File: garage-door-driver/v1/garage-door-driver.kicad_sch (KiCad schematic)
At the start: 5 parts, among them J1 Screw_Terminal_01x04

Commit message: wip sch
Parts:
- removed D1: LED_ARGB, mylife-footprints:LED RGB 10W, symbol Device:LED_ARGB
- removed J1: Screw_Terminal_01x04, mylife-footprints:RS PRO Terminal Small x4, symbol Connector:Screw_Terminal_01x04
- removed R1, R2: 5.1Ω/1W, Resistor_SMD:R_2512_6332Metric, symbol Device:R
- removed R3: 10Ω/1W, Resistor_SMD:R_2512_6332Metric, symbol Device:R
- added J1, J3: Screw_Terminal_01x02, symbol Connector:Screw_Terminal_01x02
- added J2: Conn_01x07_Pin, symbol Connector:Conn_01x07_Pin
- added U1: WeMos_D1_mini, Module:WEMOS_D1_mini_light, symbol MCU_Module:WeMos_D1_mini
- added U2: 4N35, Package_DIP:DIP-6_W7.62mm, symbol Isolator:4N35

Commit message: sch
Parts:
- added D1, D2, D3, D4, D5: LED, Diode_SMD:D_0805_2012Metric, symbol Device:LED
- added J4: Conn_01x03_Male, Connector_PinHeader_2.54mm:PinHeader_1x03_P2.54mm_Vertical, symbol Connector:Conn_01x03_Male
- added R1, R12, R13, R6, R8: 1KΩ, Resistor_SMD:R_0603_1608Metric, symbol Device:R
- added R10, R11, R4: 2.2KΩ, Resistor_SMD:R_0603_1608Metric, symbol Device:R
- added R14, R3: 220Ω, Resistor_SMD:R_0603_1608Metric, symbol Device:R
- added R2, R7, R9: 10KΩ, Resistor_SMD:R_0603_1608Metric, symbol Device:R
- added R5: 4.7KΩ, Resistor_SMD:R_0402_1005Metric, symbol Device:R
- added U3, U4, U5, U6: 4N35, Package_DIP:DIP-6_W7.62mm, symbol Isolator:4N35
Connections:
- net at J3.1 (Pin_1): now also R10.1
- net at J3.2 (Pin_2): now also U4.2
- net at U2.1: now also R4.2
- net at U2.2: now also J1.1 (Pin_1), R11.1
- net GND: now reaches U2.4
- net GND: now also U1.10 (GND), J4.1 (Pin_1), R12.1, R13.1, U3.4, U4.4, U5.2, U5.4, U6.2, U6.4
- net at U2.5: now also U1.4 (SCK/D5), R1.1, R2.1
- net at J1.2 (Pin_2): now also R4.1, U3.2
- net at U1.11 (D4): now also D5.2 (A), R3.1
- net at U1.12 (D3): now also D4.2 (A), R14.1
- net at U1.15 (RX): now also J4.3 (Pin_3), R5.2
- net at U1.5 (MISO/D6): now also R6.1, R7.1, U3.5
- net at U1.6 (MOSI/D7): now also R8.1, R9.1, U4.5
- net +3V3: now reaches U1.8 (3V3)
- net +3V3: now also D1.2 (A), D2.2 (A), D3.2 (A), J4.2 (Pin_2), R2.2, R5.1, R7.2, R9.2
- net +5V: now reaches U1.9 (5V)
- new net: R3.2, U6.1
- new net: R11.2, U3.1
- new net: D1.1 (K), R1.2
- new net: D3.1 (K), R8.2
- new net: D2.1 (K), R6.2
- new net: D5.1 (K), R13.2
- new net: R10.2, U4.1
- new net: D4.1 (K), R12.2
- new net: R14.2, U5.1
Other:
- note added: "24v"
- note added: "Bornier noir"
- note added: "DS18B20"
- note added: "GND"
- note added: "Moteur"
- note added: "VCC"
- note added: "data"
- moved on the sheet: J1, J2, J3, U1, U2

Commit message: sch
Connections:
- net GND: now also J2.1 (Pin_1)
- net at U6.5: now also J2.3 (Pin_3)
- net +24V: now reaches J2.5 (Pin_5)
- net at J2.7 (Pin_7): now also U5.5
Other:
- note added: "20 21 5 23"
- note added: "Bornier droite"
- note added: "D5 : in moteur (active low) D6 : in moteur (active low) D7 : in porte fermée (active low) D3 : out ouverture partielle D4 : out ouverture totale RX : DS18B20"
- moved on the sheet: J4, R5

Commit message: sch
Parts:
- added C1: 10μF/50V, Capacitor_SMD:C_1206_3216Metric, symbol Device:C_Polarized
- added C2: 22μF/10V, Capacitor_SMD:C_0805_2012Metric, symbol Device:C_Polarized
- added U7: R-785.0-1.0, Converter_DCDC:Converter_DCDC_RECOM_R-78E-0.5_THT, symbol Regulator_Switching:R-785.0-1.0
- U2, U3, U4, U5, U6: footprint Package_DIP:DIP-6_W7.62mm -> Package_DIP:DIP-6_W8.89mm_SMDSocket_LongPads; LCSC (none) -> C500385
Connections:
- net +24V: now also C1.1, U7.1 (IN)
- net +5V: now also C2.1, U7.3 (OUT)
- net GND: now also C1.2, C2.2, U7.2 (GND)

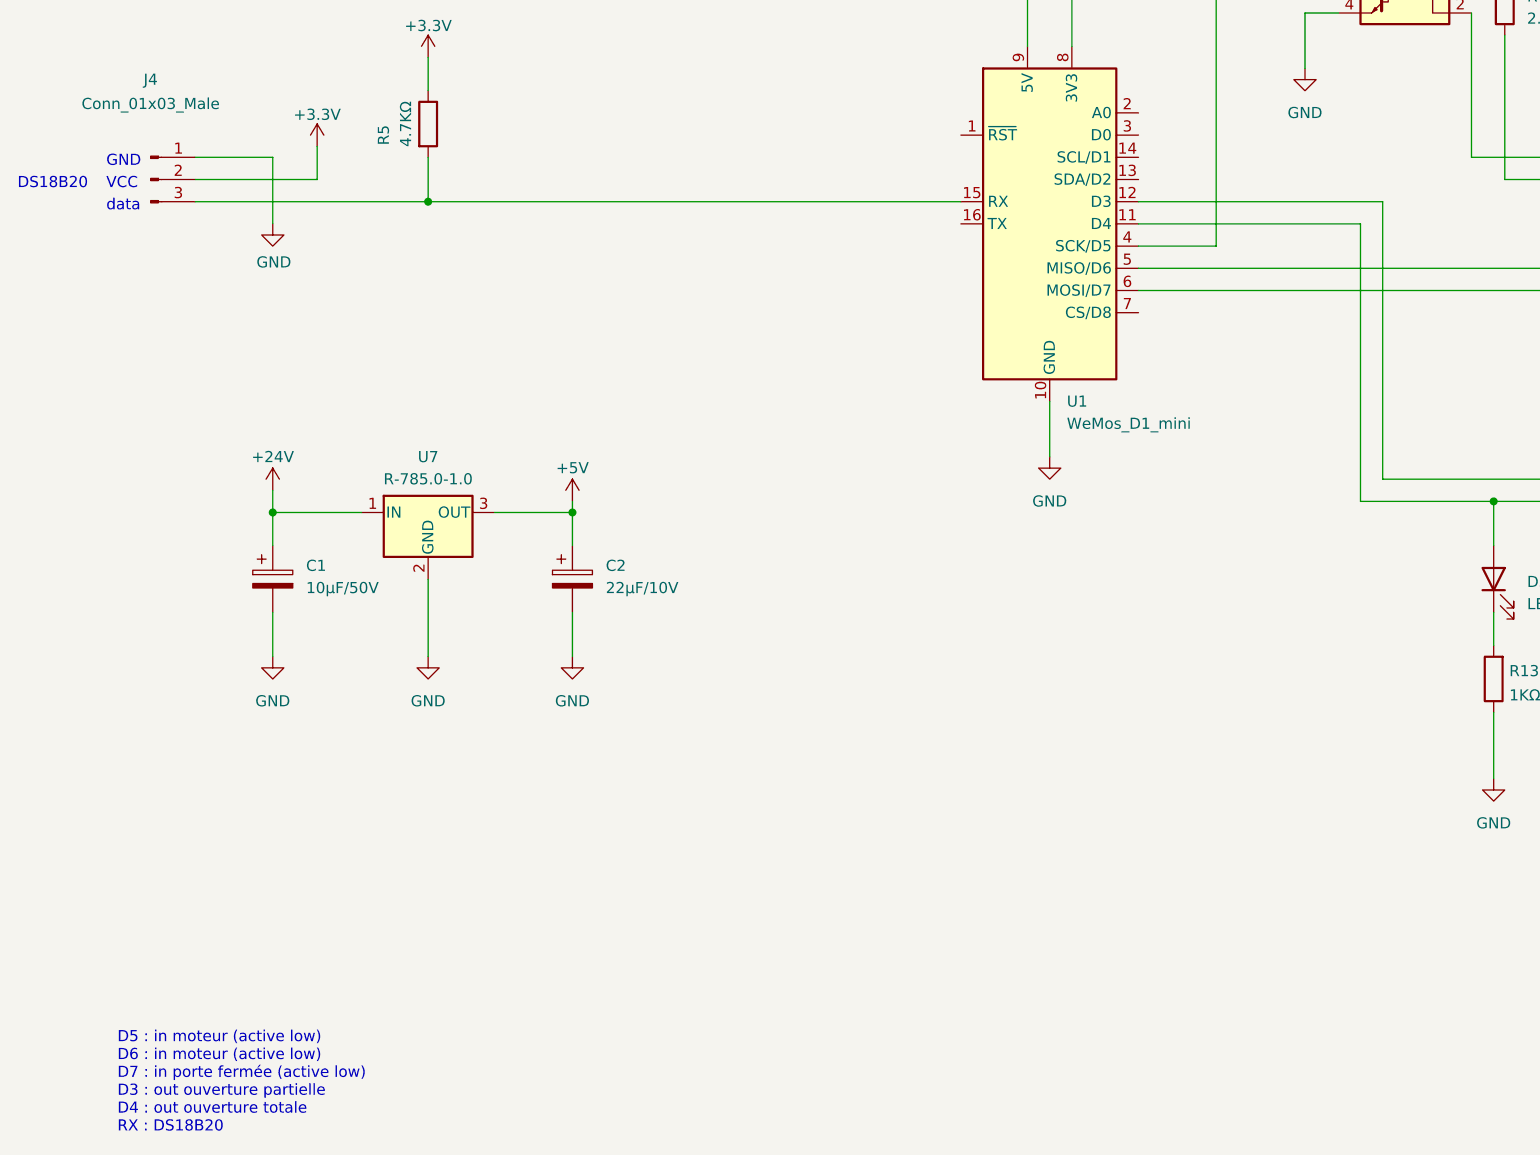
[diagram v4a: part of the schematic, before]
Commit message: fix esp8366 used pins
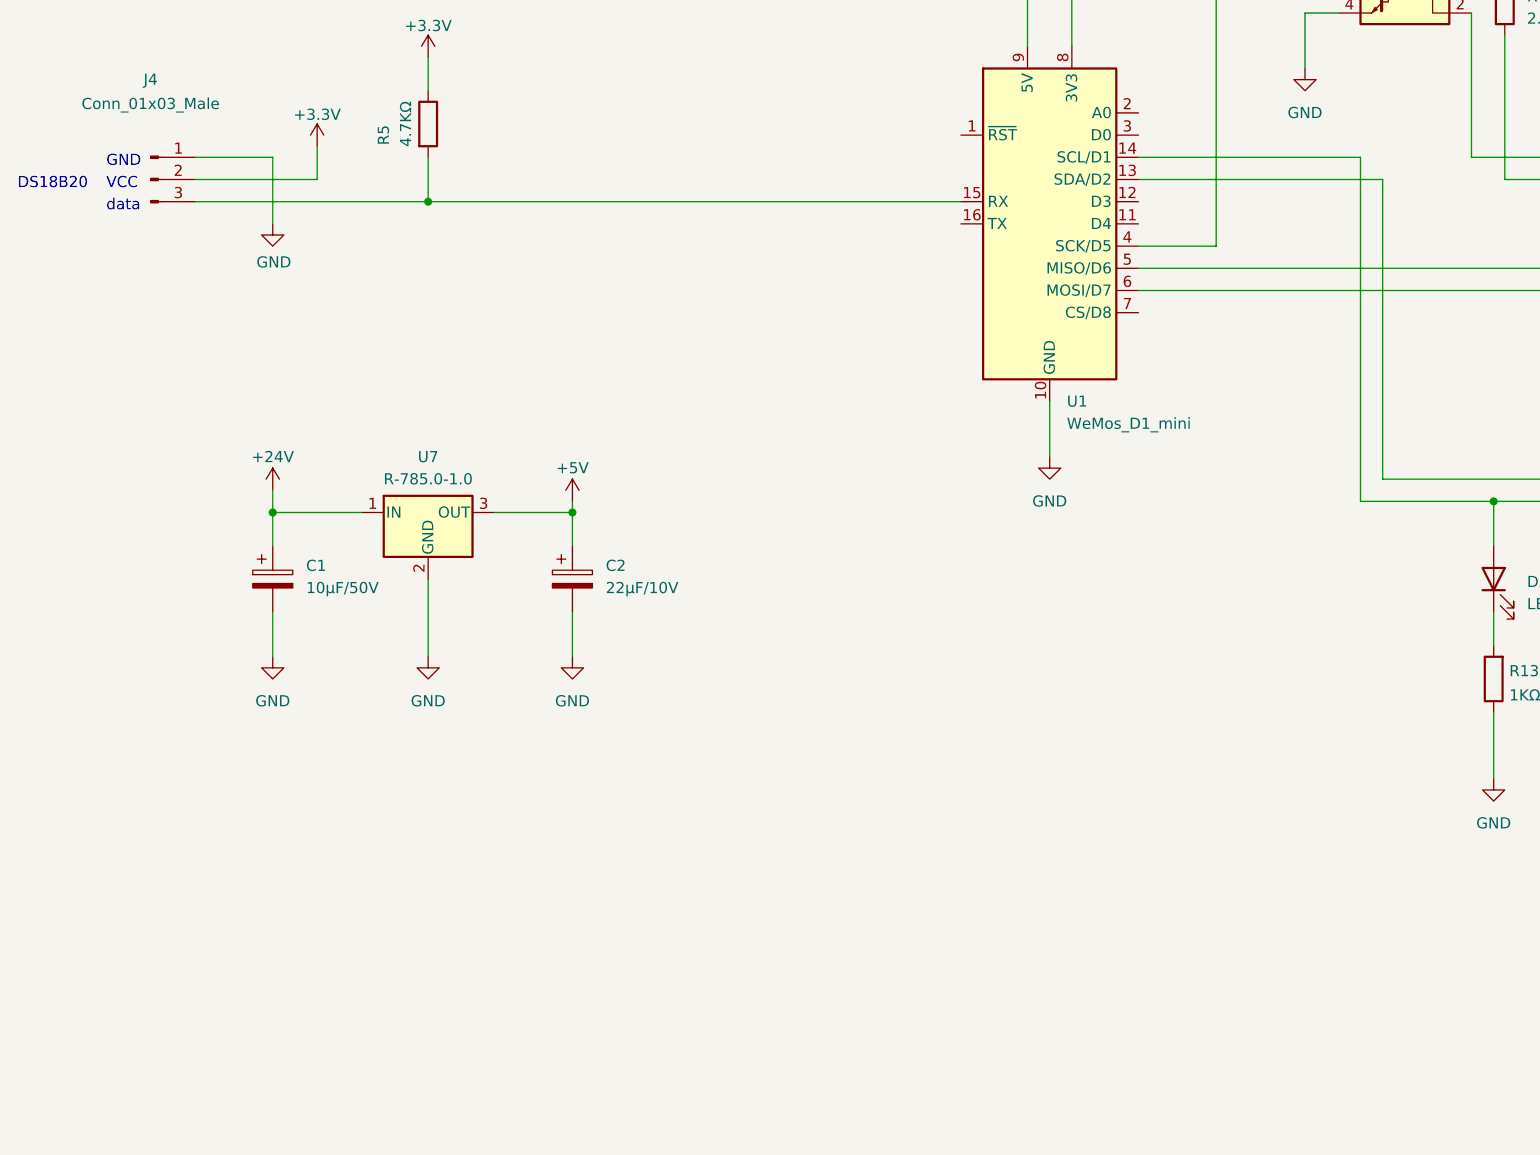
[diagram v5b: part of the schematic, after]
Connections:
- net at D5.2 (A), R3.1: now also U1.14 (SCL/D1); no longer U1.11 (D4)
- net at D4.2 (A), R14.1: now also U1.13 (SDA/D2); no longer U1.12 (D3)
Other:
- note removed: "D5 : in moteur (active low) D6 : in moteur (active low) D7 : in porte fermée (active low) D3 : out ouverture partielle D4 : out ouverture totale RX : DS18B20"
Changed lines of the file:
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@@
+    (stroke (width 0) (type default))
+  )
+  (wire (pts (xy 161.29 91.44) (xy 186.69 91.44))
     (stroke (width 0) (type default))
   )
@@
     (stroke (width 0) (type default))
   )
-  (wire (pts (xy 189.23 96.52) (xy 189.23 128.27))
-    (stroke (width 0) (type default))
-  )
   (wire (pts (xy 213.36 67.31) (xy 213.36 63.5))
     (stroke (width 0) (type default))
@@
     (stroke (width 0) (type default))
   )
+  (wire (pts (xy 189.23 93.98) (xy 189.23 128.27))
+    (stroke (width 0) (type default))
+  )
   (wire (pts (xy 302.26 93.98) (xy 242.57 93.98))
     (stroke (width 0) (type default))
@@
     (stroke (width 0) (type default))
   )
-  (wire (pts (xy 186.69 99.06) (xy 186.69 130.81))
+  (wire (pts (xy 186.69 91.44) (xy 186.69 130.81))
     (stroke (width 0) (type default))
   )
@@
     (stroke (width 0) (type default))
   )
+  (wire (pts (xy 161.29 93.98) (xy 189.23 93.98))
+    (stroke (width 0) (type default))
+  )
   (wire (pts (xy 96.52 143.51) (xy 96.52 148.59))
     (stroke (width 0) (type default))
@@
     (stroke (width 0) (type default))
   )
-  (wire (pts (xy 161.29 99.06) (xy 186.69 99.06))
-    (stroke (width 0) (type default))
-  )
   (wire (pts (xy 256.54 106.68) (xy 256.54 67.31))
     (stroke (width 0) (type default))
@@
     (stroke (width 0) (type default))
   )
-  (wire (pts (xy 161.29 96.52) (xy 189.23 96.52))
-    (stroke (width 0) (type default))
-  )
   (wire (pts (xy 304.8 128.27) (xy 285.75 128.27))
     (stroke (width 0) (type default))
@@
     (effects (font (size 1.27 1.27)) (justify left bottom))
   )
-  (text "D5 : in moteur (active low)\nD6 : in moteur (active low)\nD7 : in porte fermée (active low)\nD3 : out ouverture partielle\nD4 : out ouverture totale\nRX : DS18B20"
-    (at 44.45 203.2 0)
-    (effects (font (size 1.27 1.27)) (justify left bottom))
-  )

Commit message: annotate
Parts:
- renumbered D5 to D2, D2 to D3, D3 to D5, J4 to J1, J3 to J2, J1 to J3, J2 to J4, R5 to R1, R11 to R10, R14 to R11, R8 to R12, R9 to R13, R10 to R14, R1 to R2, R2 to R3, R13 to R4, R4 to R5, R3 to R7, R7 to R8, R12 to R9, U7 to U1, U1 to U2, U2 to U3, U6 to U4, U3 to U5, U5 to U6, U4 to U7

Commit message: pcb
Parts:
- J2, J3: footprint (none) -> mylife-footprints:RS PRO Terminal Small x2
- J4: footprint (none) -> Connector_PinHeader_2.54mm:PinHeader_1x07_P2.54mm_Vertical
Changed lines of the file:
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@@
       (effects (font (size 1.27 1.27)) (justify left))
     )
-    (property "Footprint" "" (at 307.34 69.85 0)
-      (effects (font (size 1.27 1.27)) hide)
-    )
-    (property "Datasheet" "~" (at 307.34 69.85 0)
+    (property "Footprint" "mylife-footprints:RS PRO Terminal Small x2" (at 307.34 69.85 0)
+      (effects (font (size 1.27 1.27)) hide)
+    )
+    (property "Datasheet" "https://docs.rs-online.com/90f4/0900766b8157c7e9.pdf" (at 307.34 69.85 0)
       (effects (font (size 1.27 1.27)) hide)
     )
@@
       (effects (font (size 1.27 1.27)))
     )
-    (property "Footprint" "" (at 309.88 135.89 0)
+    (property "Footprint" "Connector_PinHeader_2.54mm:PinHeader_1x07_P2.54mm_Vertical" (at 309.88 135.89 0)
       (effects (font (size 1.27 1.27)) hide)
     )
@@
       (effects (font (size 1.27 1.27)) (justify left))
     )
-    (property "Footprint" "" (at 307.34 91.44 0)
-      (effects (font (size 1.27 1.27)) hide)
-    )
-    (property "Datasheet" "~" (at 307.34 91.44 0)
-      (effects (font (size 1.27 1.27)) hide)
-    )
+    (property "Footprint" "mylife-footprints:RS PRO Terminal Small x2" (at 307.34 91.44 0)
+      (effects (font (size 1.27 1.27)) hide)
+    )
+    (property "Datasheet" "https://docs.rs-online.com/90f4/0900766b8157c7e9.pdf" (at 307.34 91.44 0)
+      (effects (font (size 1.27 1.27)) hide)
+    )
